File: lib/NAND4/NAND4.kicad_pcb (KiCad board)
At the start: 2 copper layers, 8 parts

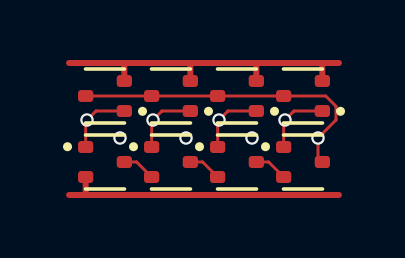
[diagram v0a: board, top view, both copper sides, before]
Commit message: All cells now use 1mm*4mm grid rather than 1.1mm*4.4mm
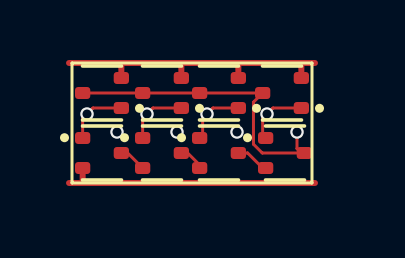
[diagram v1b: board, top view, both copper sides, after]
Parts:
- moved P4 0.71 mm to (7.00, 1.00)
- moved N4 0.67 mm to (7.10, 3.00)
- moved N3 0.67 mm to (4.90, 3.00)
- moved P3 0.61 mm to (4.90, 1.00)
- moved N2 0.42 mm to (3.00, 3.00)
- moved N1 0.32 mm to (1.00, 3.00)
- moved P2 0.32 mm to (3.00, 1.00)
- moved P1 0.14 mm to (1.00, 1.00)
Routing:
- net VDD: track 11.4 -> 10.3 mm
- net GND: track 9.60 -> 8.72 mm

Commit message: Make the pads of my SOT523 footprint very slightly smaller, which is enough to route all the cells and leave the mosfets exactly on the grid
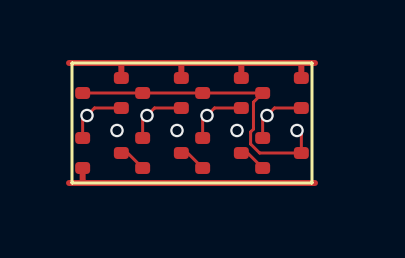
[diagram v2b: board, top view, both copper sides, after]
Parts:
- N1, N2, N3, N4, P1, P2, P3, P4: footprint Package_TO_SOT_SMD:SOT-523 -> RV523:SOT523
- moved N3 0.10 mm to (5.00, 3.00)
- moved N4 0.10 mm to (7.00, 3.00)
- moved P3 0.10 mm to (5.00, 1.00)

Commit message: Propagate MOSFET values to the cells' PCBs
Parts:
- N1, N2, N3, N4: value (none) -> NMOS
- P1, P2, P3, P4: value (none) -> PMOS
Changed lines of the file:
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@@
 			)
 		)
-		(property "Value" ""
+		(property "Value" "PMOS"
 			(at 0 0 180)
 			(layer "F.Fab")
@@
 			)
 		)
-		(property "Value" ""
+		(property "Value" "PMOS"
 			(at 0 0 180)
 			(layer "F.Fab")
@@
 			)
 		)
-		(property "Value" ""
+		(property "Value" "PMOS"
 			(at 0 0 180)
 			(layer "F.Fab")
@@
 			)
 		)
-		(property "Value" ""
+		(property "Value" "NMOS"
 			(at 0 0 0)
 			(layer "F.Fab")
@@
 			)
 		)
-		(property "Value" ""
+		(property "Value" "PMOS"
 			(at 0 0 180)
 			(layer "F.Fab")
@@
 			)
 		)
-		(property "Value" ""
+		(property "Value" "NMOS"
 			(at 0 0 0)
 			(layer "F.Fab")
@@
 			)
 		)
-		(property "Value" ""
+		(property "Value" "NMOS"
 			(at 0 0 0)
 			(layer "F.Fab")
@@
 			)
 		)
-		(property "Value" ""
-			(at 0 0 0)
-			(layer "F.Fab")
+		(property "Value" "NMOS"
+			(at 0 0 0)
+			(layer "F.Fab")
